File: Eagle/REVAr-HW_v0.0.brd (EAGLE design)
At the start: 101.6 x 53.3 mm, 100 parts, among them IC1 MC33269ST-5.0T3, IC2 MC33269D-5.0, IC3 ATMEGA2560-16AU, IC4 ATMEGA8U2-MU, IC5 LM358D, IC6 LP2985-33DBVR, IC7 PCF8574T, Q1 16MHz, Q2 16MHz, T2 FDN340P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

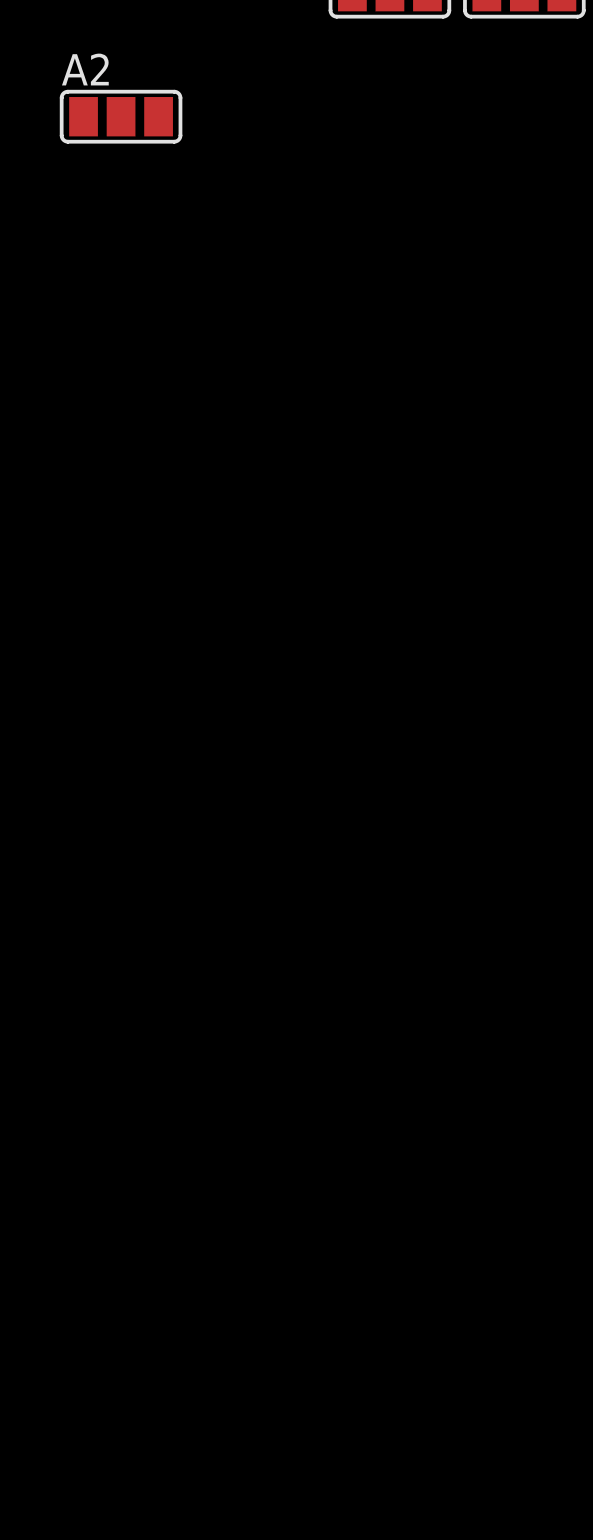
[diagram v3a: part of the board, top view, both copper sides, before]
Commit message: [HW] Add push buttons for user interface
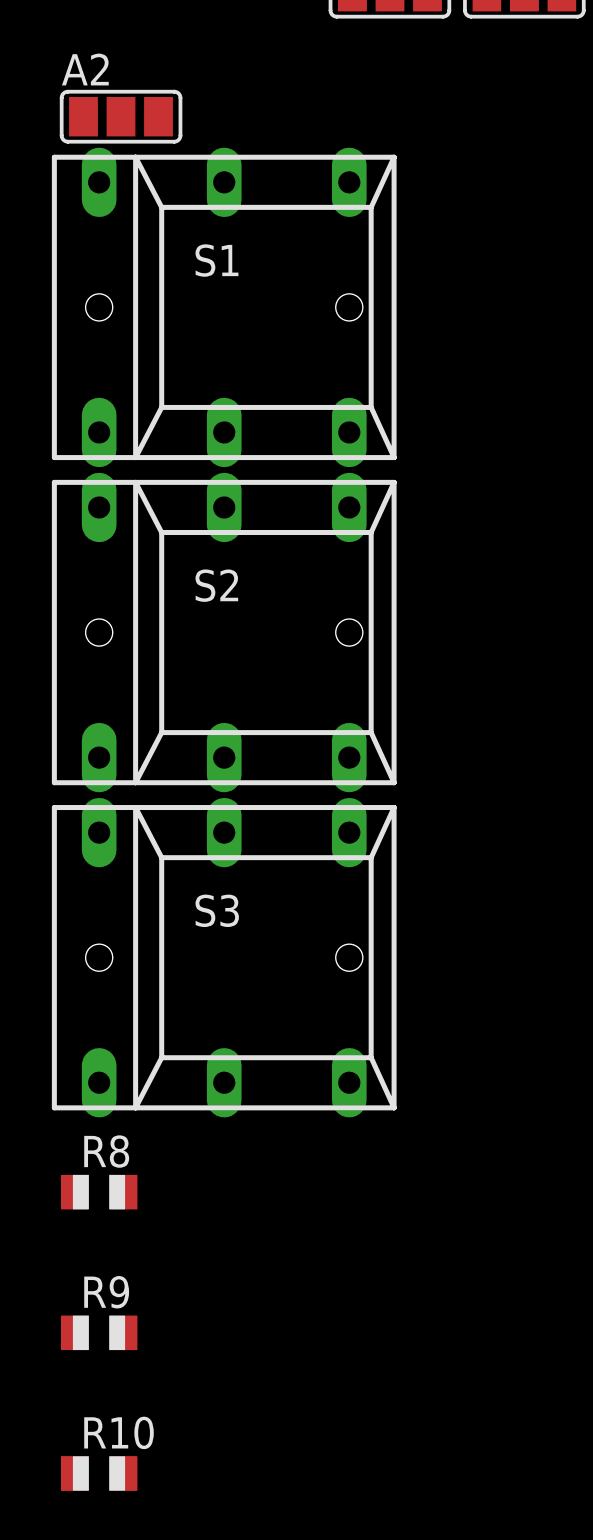
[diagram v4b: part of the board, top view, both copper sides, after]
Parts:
- added R10, R8, R9: 10k, adafruit:R0805
- added S1, S2, S3: (no value), switch:REKN
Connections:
- net +5V: now also LCD_1-6.2
- net GND: now also S1.0A, S2.0A, S3.0A
- net PB5: now also R8.1, S1.1A
- net PB6: now also R9.1, S2.1A
- net PB7: now also R10.1, S3.1A
- net VCC: now also R10.2, R8.2, R9.2; no longer LCD_1-6.2

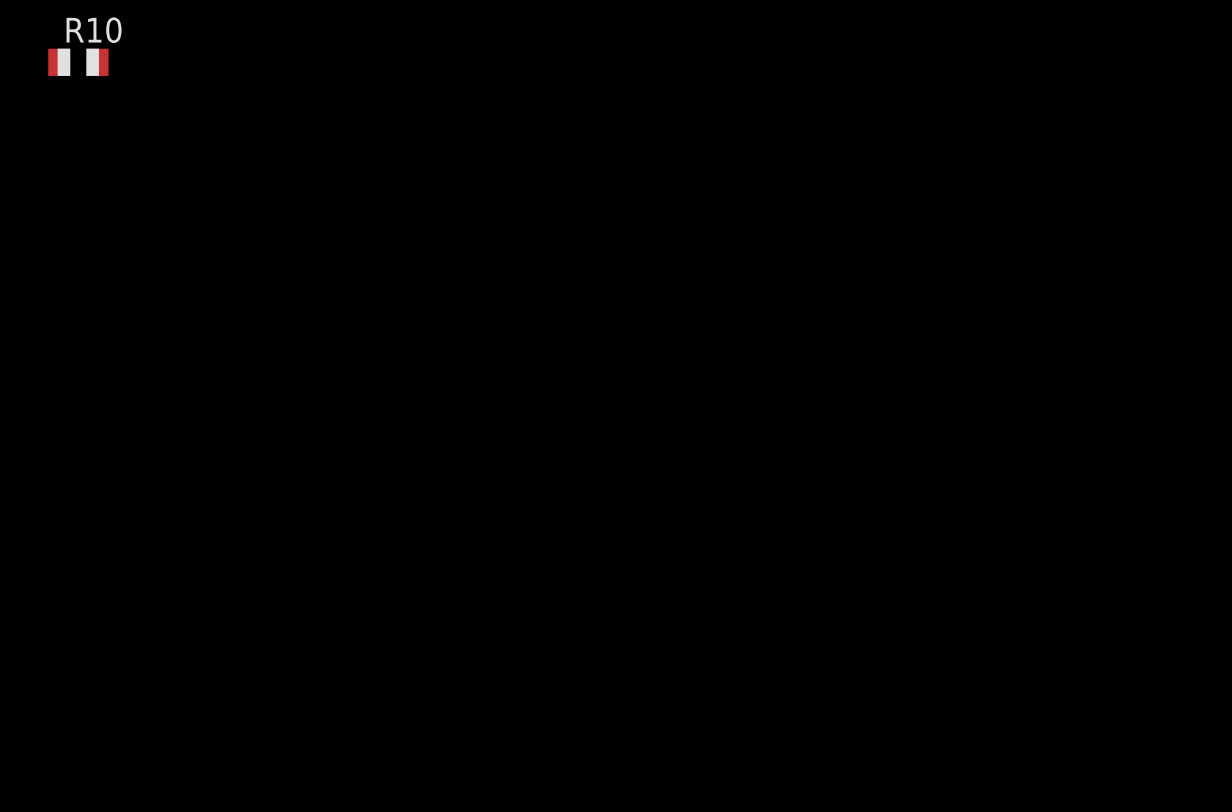
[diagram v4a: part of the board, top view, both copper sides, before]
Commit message: [HW] Add SD Card Adapter
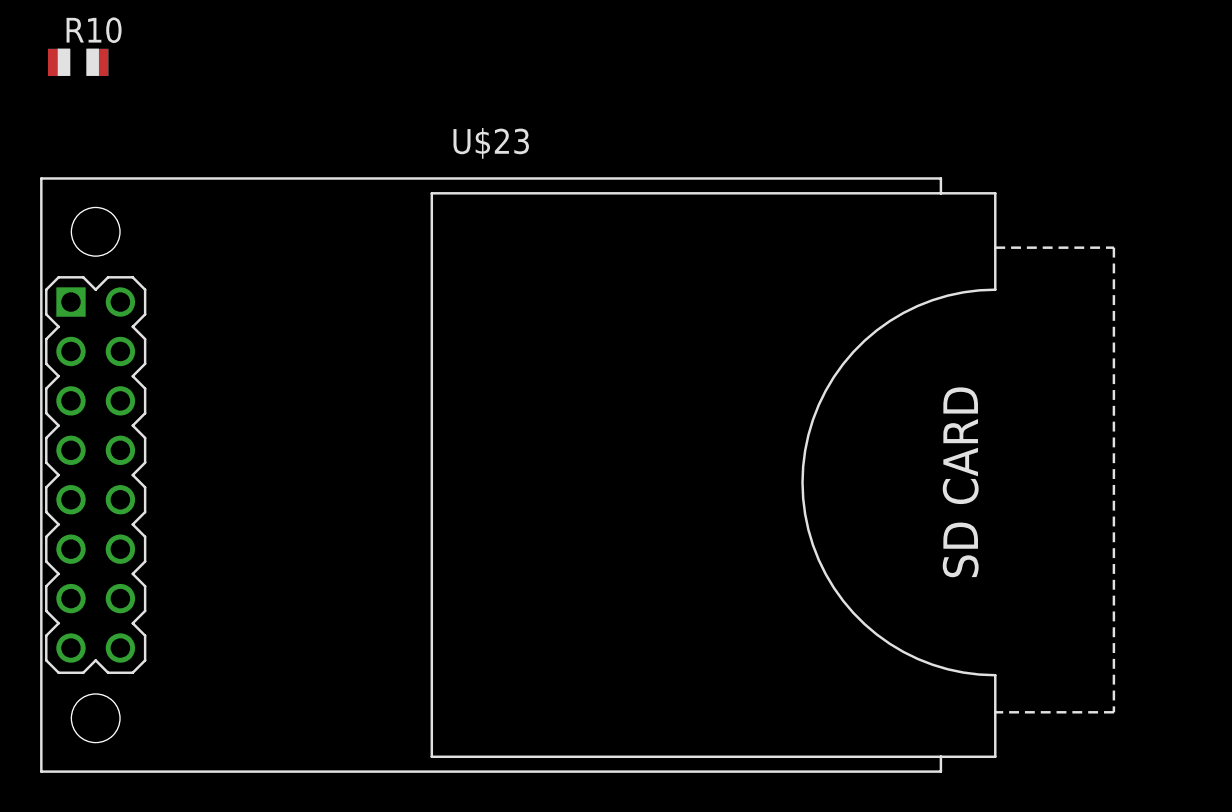
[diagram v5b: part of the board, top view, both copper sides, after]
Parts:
- added U$23: CARD-SD-ADAPTER, diy-modules:CARD-SD-ADAPTER
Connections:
- new net 3V3: U$23.3
- new net N$18: U$23.7
- net GND: now also U$23.1, U$23.15
- net PB1: now also U$23.11
- net PB2: now also U$23.9
- net PB3: now also U$23.13
- net VCC: now also U$23.5
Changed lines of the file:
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@@
 <element name="R9" library="adafruit" package="R0805" value="10k" x="-95.631" y="-470.789"/>
 <element name="R10" library="adafruit" package="R0805" value="10k" x="-95.631" y="-476.504"/>
+<element name="U$23" library="diy-modules" package="CARD-SD-ADAPTER" value="CARD-SD-ADAPTER" x="-74.422" y="-497.713"/>
 </elements>
 <signals>
@@
 <contactref element="S2" pad="0A"/>
 <contactref element="S3" pad="0A"/>
+<contactref element="U$23" pad="1"/>
+<contactref element="U$23" pad="15"/>
 <wire x1="-85.344" y1="-416.306" x2="-85.471" y2="-424.053" width="0" layer="19" extent="1-1"/>
 <wire x1="-83.058" y1="-411.734" x2="-85.344" y2="-416.306" width="0" layer="19" extent="1-1"/>
@@
 <wire x1="-54.229" y1="-235.458" x2="-54.229" y2="-266.827" width="0" layer="19" extent="1-1"/>
 <wire x1="-81.661" y1="-250.571" x2="-54.229" y2="-235.458" width="0" layer="19" extent="1-1"/>
+<wire x1="-96.012" y1="-488.823" x2="-85.471" y2="-450.469" width="0" layer="19" extent="1-1"/>
+<wire x1="-96.012" y1="-506.603" x2="-96.012" y2="-488.823" width="0" layer="19" extent="1-1"/>
 <wire x1="-78.994" y1="-185.293" x2="-54.229" y2="-235.458" width="0" layer="19" extent="1-1"/>
 <wire x1="13.589" y1="-69.85" x2="-78.994" y2="-185.293" width="0" layer="19" extent="1-1"/>
@@
 <via x="49.022" y="8.636" extent="1-16" drill="0.4064" shape="octagon"/>
 <via x="81.026" y="8.763" extent="1-16" drill="0.4064" shape="octagon"/>
+<contactref element="U$23" pad="13"/>
+<wire x1="48.768" y1="8.636" x2="-96.012" y2="-504.063" width="0" layer="19" extent="16-16"/>
 </signal>
 <signal name="PB2">
@@
 <via x="50.673" y="10.125" extent="1-16" drill="0.4064" shape="octagon"/>
 <via x="75.819" y="10.16" extent="1-16" drill="0.4064" shape="octagon"/>
+<contactref element="U$23" pad="9"/>
+<wire x1="48.768" y1="9.398" x2="-96.012" y2="-498.983" width="0" layer="19" extent="16-16"/>
 </signal>
 <signal name="PB1">
@@
 <via x="40.894" y="25.146" extent="1-16" drill="0.4064" shape="octagon"/>
 <via x="49.23" y="10.287" extent="1-16" drill="0.4064" shape="octagon"/>
+<contactref element="U$23" pad="11"/>
+<wire x1="48.768" y1="10.287" x2="-96.012" y2="-501.523" width="0" layer="19" extent="16-16"/>
 </signal>
 <signal name="PB5">
@@
 <contactref element="R8" pad="2"/>
 <contactref element="R10" pad="2"/>
+<contactref element="U$23" pad="5"/>
 <wire x1="-89.932" y1="-400.177" x2="-96.631" y2="-400.177" width="0" layer="19" extent="1-1"/>
 <wire x1="-85.233" y1="-400.177" x2="-89.932" y2="-400.177" width="0" layer="19" extent="1-1"/>
@@
 <wire x1="-94.631" y1="-470.789" x2="-94.631" y2="-465.074" width="0" layer="19" extent="1-1"/>
 <wire x1="-94.631" y1="-476.504" x2="-94.631" y2="-470.789" width="0" layer="19" extent="1-1"/>
+<wire x1="-96.012" y1="-493.903" x2="-94.631" y2="-476.504" width="0" layer="19" extent="1-1"/>
 <wire x1="-73.914" y1="-185.293" x2="-54.229" y2="-227.838" width="0" layer="19" extent="1-1"/>
 <wire x1="-11.176" y1="-49.784" x2="-73.914" y2="-185.293" width="0" layer="19" extent="1-1"/>
@@
 <wire x1="-94.742" y1="-421.386" x2="-92.075" y2="-396.141" width="0" layer="19" extent="1-1"/>
 </signal>
+<signal name="3V3">
+<contactref element="U$23" pad="3"/>
+</signal>
+<signal name="N$18">
+<contactref element="U$23" pad="7"/>
+</signal>
 </signals>

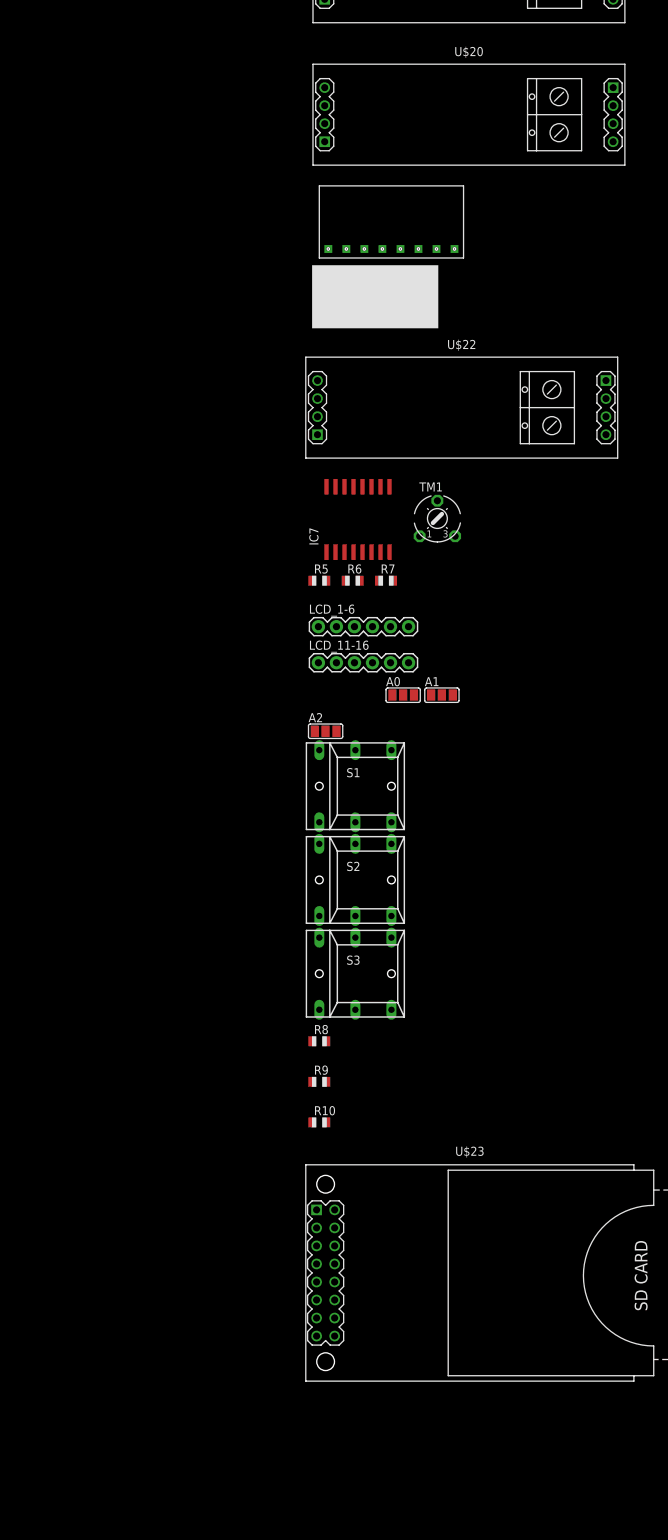
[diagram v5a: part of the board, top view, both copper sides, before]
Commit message: [HW] Add BMP280 and DS1307 to design
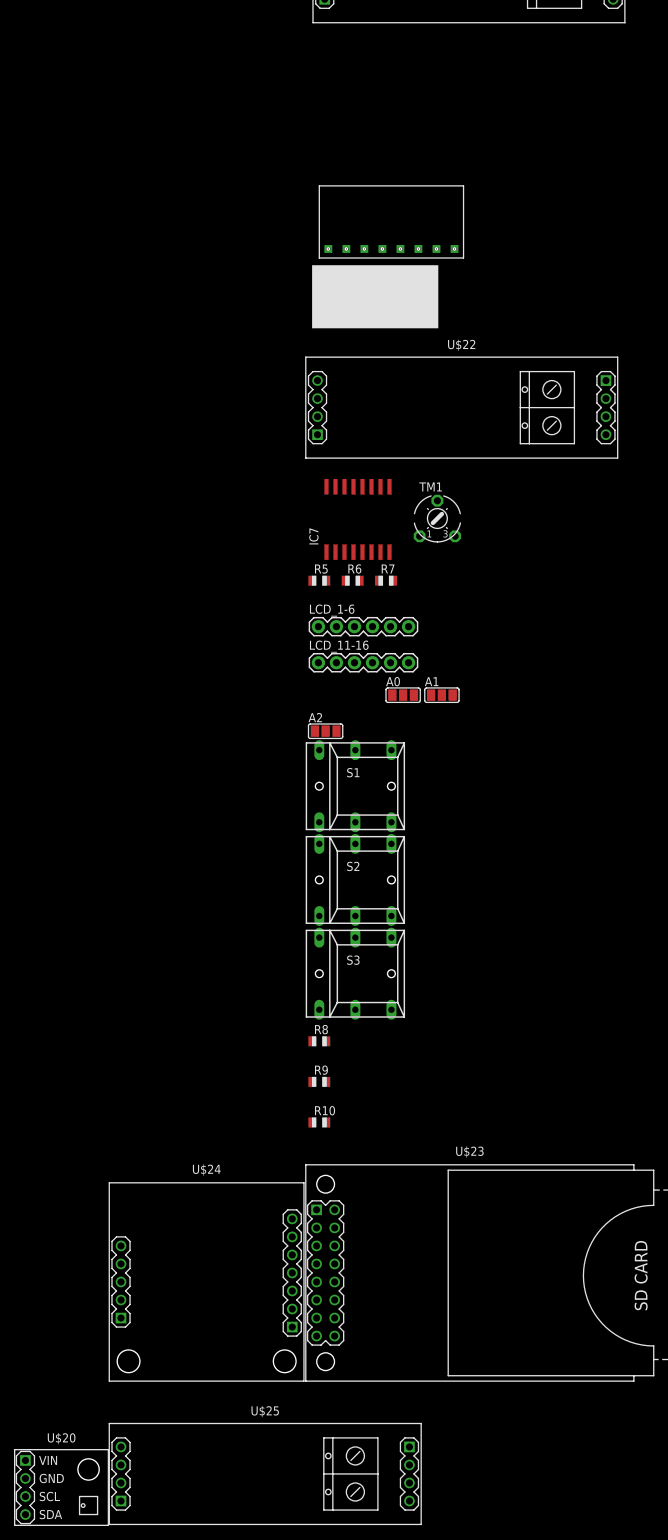
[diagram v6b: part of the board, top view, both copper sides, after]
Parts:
- added U$24: RTC-EEPROM-BATTERY, diy-modules:RTC-EEPROM-BATTERY
- added U$25: RS485-TTL-CONVERTER, diy-modules:RS485-TTL-CONVERTER
- U$20: value RS485-TTL-CONVERTER -> TEMP-HUM-PRES-BME280; device diy-modules:RS485-TTL-CONVERTER -> diy-modules:TEMP-HUM-PRES-BME280
- moved U$20 201.8 mm to (-132.0, -527.9)
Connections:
- new net GND.2: U$24.J2.2
- new net VCC.2: U$24.J2.3
- net A-485: now also U$25.J2.3; no longer U$20.J2.3
- net B-485: now also U$25.J2.2; no longer U$20.J2.2
- net GND: now also U$20.2, U$24.J1.1, U$25.J2.4; no longer U$20.J2.4
- net PH6: now also U$25.J1.2, U$25.J1.3; no longer U$20.J1.2, U$20.J1.3
- net RXD2: now also U$25.J1.4; no longer U$20.J1.4
- net SCL: now also U$20.3, U$24.J1.4
- net SDA: now also U$20.4, U$24.J1.3
- net TXD2: now also U$25.J1.1; no longer U$20.J1.1
- net VCC: now also U$20.1, U$24.J1.2, U$25.J2.1; no longer U$20.J2.1
